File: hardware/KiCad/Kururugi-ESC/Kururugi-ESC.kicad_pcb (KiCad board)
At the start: 6 copper layers, 37.9 x 23.6 mm, 142 parts, among them J1 Conn_01x01, J10 Conn_01x01, J11 Conn_01x01, J2 Conn_01x01, J3 Conn_01x01, J4 Conn_01x01, J5 Conn_01x01, J6 JTAG_TC2030, J7 Conn_01x01, J8 Conn_01x01, J9 Conn_01x01, Q1 CSD18540Q5B, Q2 CSD18540Q5B, Q3 CSD18540Q5B, Q4 CSD18540Q5B, Q5 CSD18540Q5B, Q6 CSD18540Q5B, U1 STM32G484CEU6, U2 LM5160A, U3 TPS7B92033, U4 2EDL8024, U5 2EDL8024, U6 2EDL8024, X1 16MHz

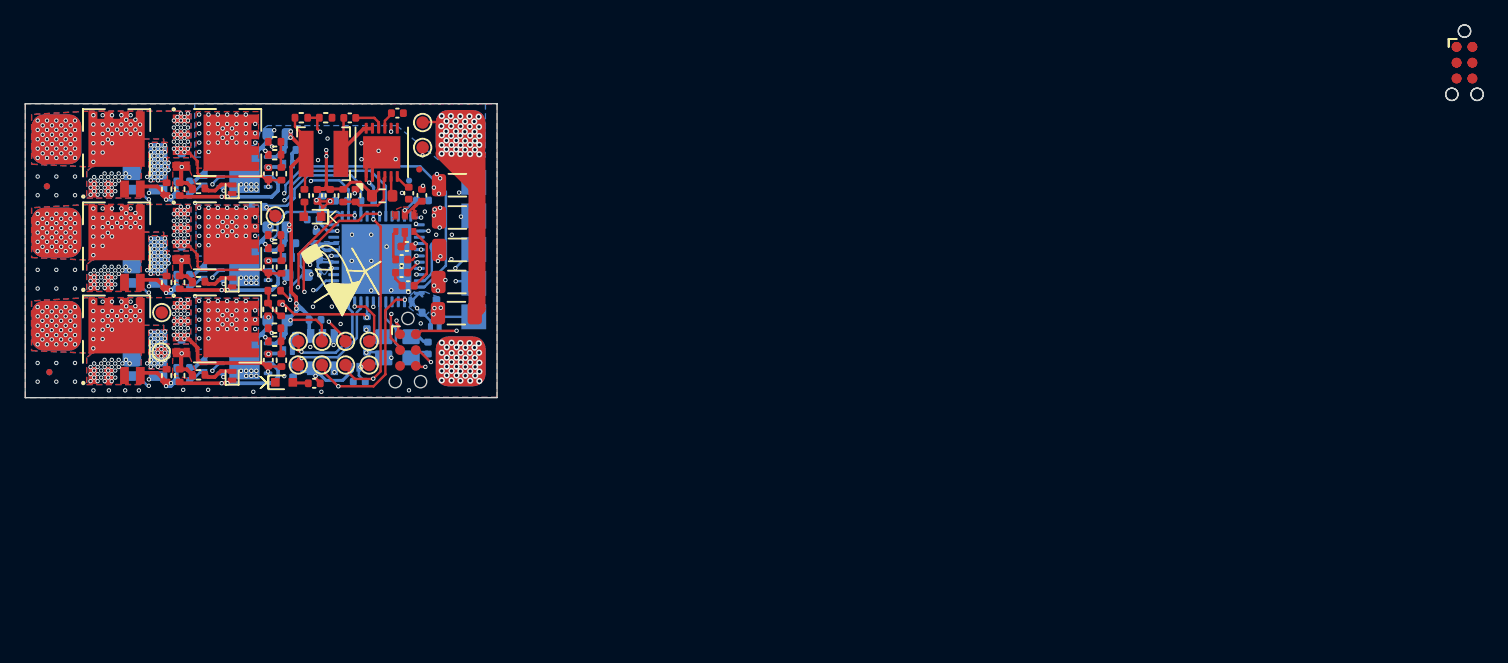
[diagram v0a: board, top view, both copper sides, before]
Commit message: Doc Update + Added CubeIDE
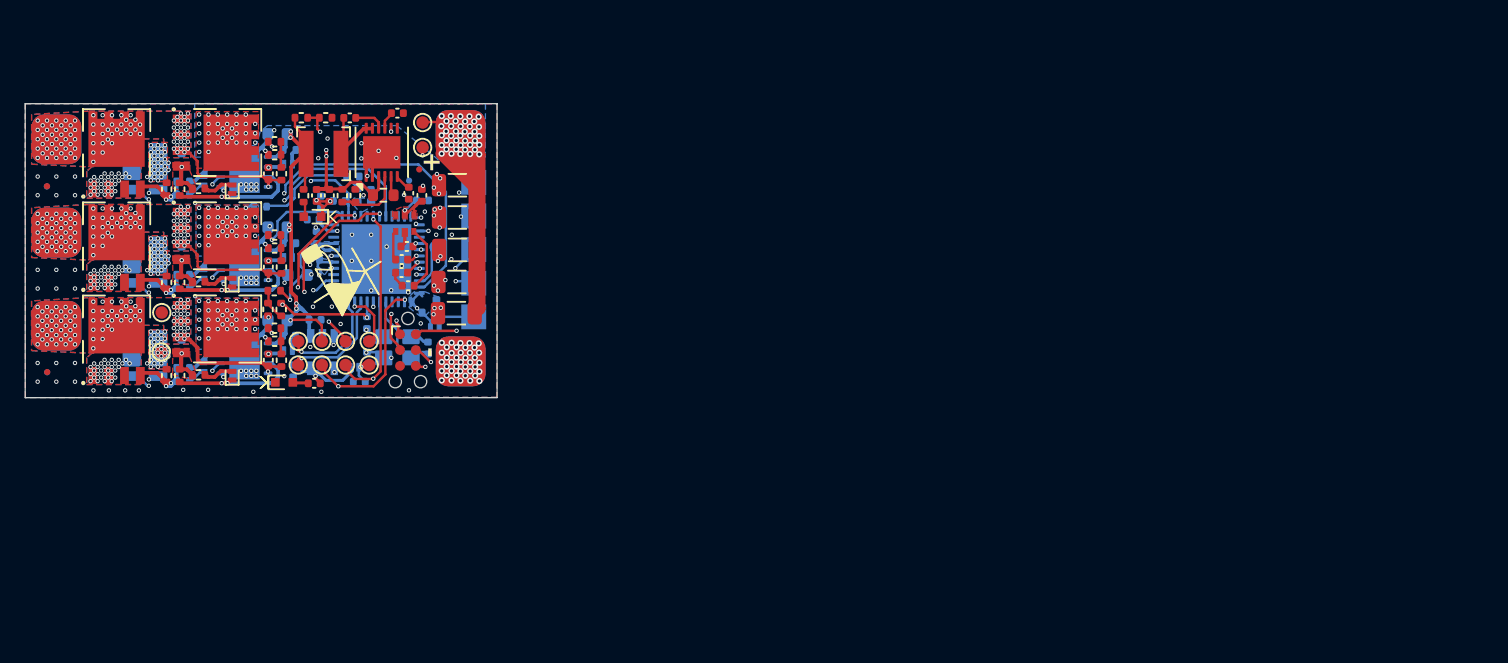
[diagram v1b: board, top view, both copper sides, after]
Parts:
- removed the J6 at (196.5, 37.7) (x2)
- removed the TP8 at (101.0, 50.0)
- added C6: 100n, KururugiESC-Footprints-Lib:C_0402_1005Metric, B.Cu at (108.7, 48.4)
- added R2: 33, KururugiESC-Footprints-Lib:R_0402_1005Metric, B.Cu at (107.6, 48.4)
- R1: value 10k -> 22k
- R3: renamed from R2; value 10k -> 1k
- moved R3 2.27 mm to (107.2, 46.9), turned to 0 degrees
- moved C27 0.18 mm to (106.1, 48.8)
- moved FID3 0.18 mm to (82.7, 62.6)
- moved FID4 0.17 mm to (82.7, 62.6)
- moved R1 0.17 mm to (99.8, 49.3), turned to 0 degrees
- moved C30 0.14 mm to (104.7, 48.9)
- moved R4 0.10 mm to (109.7, 48.4)
- moved C10 0.07 mm to (104.3, 48.4)
- moved C11 0.07 mm to (105.3, 48.4)
- moved R5 0.07 mm to (106.4, 48.4)
- moved R6 0.07 mm to (103.3, 48.4)
- renumbered C3 to C1, C9 to C10, C10 to C11, C11 to C12, C12 to C15, C15 to C16, C16 to C17, C17 to C18, C18 to C19, C4 to C2, C19 to C20, C20 to C21, C21 to C22, C22 to C23, C23 to C24, C24 to C25, C25 to C26, C26 to C27, C27 to C28, C28 to C29, C5 to C3, C29 to C30, C30 to C31, C31 to C32, C32 to C33, C6 to C4, C7 to C5, C1 to C7, C2 to C8, C8 to C9, J7 to J6, J8 to J7, J6 to J8, R9 to R10, R10 to R11, R11 to R12, R12 to R13, R13 to R14, R14 to R15, R15 to R16, R16 to R17, R17 to R18, R18 to R19, R19 to R20, R20 to R21, R21 to R22, R22 to R23, R23 to R24, R24 to R25, R25 to R26, R26 to R27, R27 to R28, R28 to R29, R29 to R30, R30 to R31, R31 to R32, R32 to R33, R33 to R34, R34 to R35, R35 to R36, R36 to R37, R37 to R38, R38 to R39, R3 to R4, R39 to R40, R40 to R41, R41 to R42, R42 to R43, R43 to R44, R44 to R45, R45 to R46, R46 to R47, R47 to R48, R48 to R49, R4 to R5, R5 to R6, R6 to R7, R7 to R8, R8 to R9, TP11 to TP10, TP12 to TP11, TP13 to TP12, TP14 to TP13, TP9 to TP8, TP10 to TP9
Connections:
- net /ISENS1_OPAMP_VOUT renamed /OPAMP_VOUT_ISENS3
- R1 pad 1: /VSENSBAT -> VBAT
- R1 pad 2: VBAT -> Net-(R1-Pad2)
- R3 pad 1: GND -> Net-(R1-Pad2)
- R3 pad 2: /VSENSBAT -> GND
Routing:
- net /VSENSBAT: track 14.3 -> 0.00 mm, vias 1 -> 0
- net Net-(R1-Pad2): track 0.00 -> 9.88 mm
- net GND: track 38.6 -> 37.1 mm
- net VBAT: track 56.1 -> 56.9 mm
- net /VSENS1: track 9.65 -> 10.3 mm
- added copper zone on B.Cu, net /VSENSBAT
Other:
- board text added: "+"
- board text added: "-"

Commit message: Kicad minor corrections
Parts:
- moved C10 16.2 mm to (112.8, 62.1)
- moved C11 16.2 mm to (113.9, 62.1)
- moved C14 16.2 mm to (120.2, 61.9)
- moved C16 16.2 mm to (112.8, 65.5)
- moved C25 16.2 mm to (109.0, 60.3)
- moved C28 16.2 mm to (109.0, 67.8)
- moved C3 16.2 mm to (124.2, 66.5)
- moved C32 16.2 mm to (109.7, 72.1)
- moved C6 16.2 mm to (117.2, 62.1)
- moved D11 16.2 mm to (110.5, 74.6)
- moved D12 16.2 mm to (106.1, 76.6)
- moved D3 16.2 mm to (115.9, 75.9)
- moved J9 16.2 mm to (91.9, 57.6)
- moved Q4 16.2 mm to (96.8, 66.3)
- moved R2 16.2 mm to (116.1, 62.1)
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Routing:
- net /TSENS: track 8.66 -> 8.58 mm, vias 2 -> 1
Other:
- rule pad_to_mask_clearance: 0 -> 0.05
- board text added: "10mm"

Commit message: G484 -> G474
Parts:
- U1: value STM32G484CEU6 -> STM32G474CEU6; footprint KururugiESC-Footprints-Lib:STM32G484CEU6 -> KururugiESC-Footprints-Lib:STM32G474CEU6
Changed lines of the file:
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@@
 			)
 		)
-		(property "LCSC" "C25752"
+		(property "LCSC" "C25105"
 			(at 0 0 0)
 			(unlocked yes)
@@
 			)
 		)
-		(property "LCSC" "C25752"
+		(property "LCSC" "C25105"
 			(at 0 0 270)
 			(unlocked yes)
@@
 			)
 		)
-		(property "LCSC" "C25752"
+		(property "LCSC" "C25105"
 			(at 0 0 0)
 			(unlocked yes)
@@
 			)
 		)
-		(property "LCSC" "C25752"
+		(property "LCSC" "C25105"
 			(at 0 0 0)
 			(unlocked yes)
@@
 		)
 	)
-	(footprint "KururugiESC-Footprints-Lib:STM32G484CEU6"
+	(footprint "KururugiESC-Footprints-Lib:STM32G474CEU6"
 		(layer "B.Cu")
 		(at 117.6475 67.21 90)
@@
 			)
 		)
-		(property "Value" "STM32G484CEU6"
+		(property "Value" "STM32G474CEU6"
 			(at 0 -4.83 90)
 			(unlocked yes)
@@
 			)
 		)
-		(property "Datasheet" "https://www.st.com/resource/en/datasheet/stm32g484ce.pdf"
+		(property "Datasheet" "https://www.st.com/resource/en/datasheet/stm32g474ce.pdf"
 			(at 0 0 90)
 			(unlocked yes)
@@
 			)
 		)
-		(property "Manufacturer Part Number" "STM32G484CEU6"
+		(property "Manufacturer Part Number" "STM32G474CEU6"
 			(at 0 0 270)
 			(unlocked yes)
@@
 			)
 		)
-		(property "Distributor Link 1" "https://au.mouser.com/ProductDetail/STMicroelectronics/STM32G484CEU6?qs=uwxL4vQweFNyvzDDAcwe0g%3D%3D&srsltid=AfmBOorGaREXAmNOcdk6r5tpCHAUqhfaZQDfcjQ4pwtXLsObWSo9UNFw"
+		(property "Distributor Link 1" "https://www.digikey.com/en/products/detail/stmicroelectronics/STM32G474CEU6/10326774"
 			(at 0 0 270)
 			(unlocked yes)
@@
 			)
 		)
-		(property "Distributor Link 2" "https://www.digikey.com.au/en/products/detail/stmicroelectronics/STM32G484CEU6/10326737?srsltid=AfmBOor8ccBcNfS8fvYv8dJtWtLX3YAXAeTByNZODy8iSdC1CzH-YSb1"
+		(property "Distributor Link 2" "https://au.mouser.com/ProductDetail/STMicroelectronics/STM32G474CEU6?qs=PzGy0jfpSMvczLLzMNbcpg%3D%3D&srsltid=AfmBOoq5JSw8SE4hHwGJsHZCTa1RTiSD5CVCrtCJyvgpauQ2grC3vdrj"
 			(at 0 0 270)
 			(unlocked yes)
@@
 			)
 		)
-		(property "LCSC" "C1342230"
+		(property "LCSC" " C1235412"
 			(at 0 0 270)
 			(unlocked yes)
@@
 		)
 		(embedded_fonts no)
-		(model "${KIPRJMOD}/Libraries/3Dmodels/STM32G484CEU6.step"
+		(model "${KIPRJMOD}/Libraries/3Dmodels/STM32G474CEU6.step"
 			(offset
 				(xyz 0 0 0)
@@
 			)
 		)
-		(property "LCSC" "C25752"
+		(property "LCSC" "C25105"
 			(at 0 0 270)
 			(unlocked yes)
